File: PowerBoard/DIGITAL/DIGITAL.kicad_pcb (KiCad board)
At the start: 2 copper layers, 50 x 75 mm, 55 parts, among them J1 AuxConn, J2 Conn_02x02_Counter_Clockwise, Q2 BSS126, Q3 IRFR13N20DTRPBF, Q4 IRFR13N20DTRPBF, U3 MT2492, U4 TL431DBZ, U5 STM32G030F6Px, U6 IR2181, U7 INA180A2

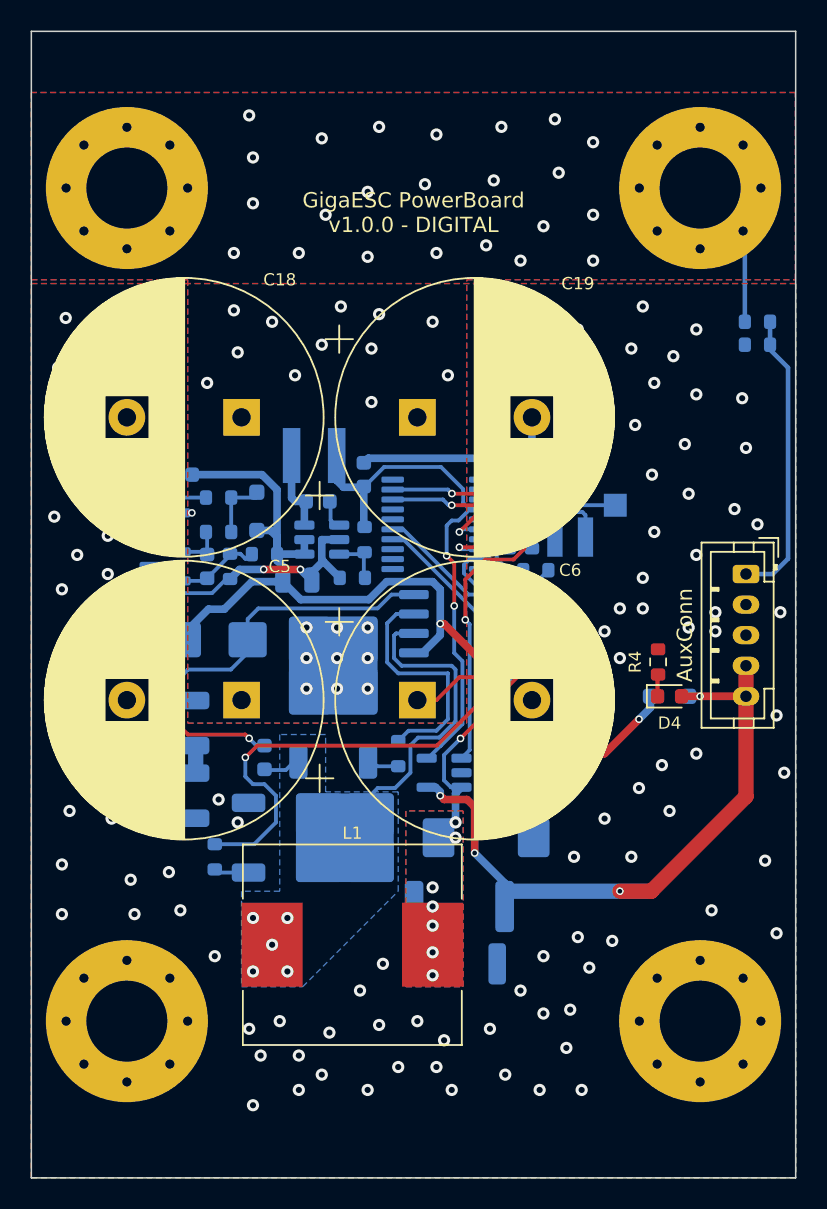
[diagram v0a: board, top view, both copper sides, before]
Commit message: v3.0.3 - Cosmetic Changes
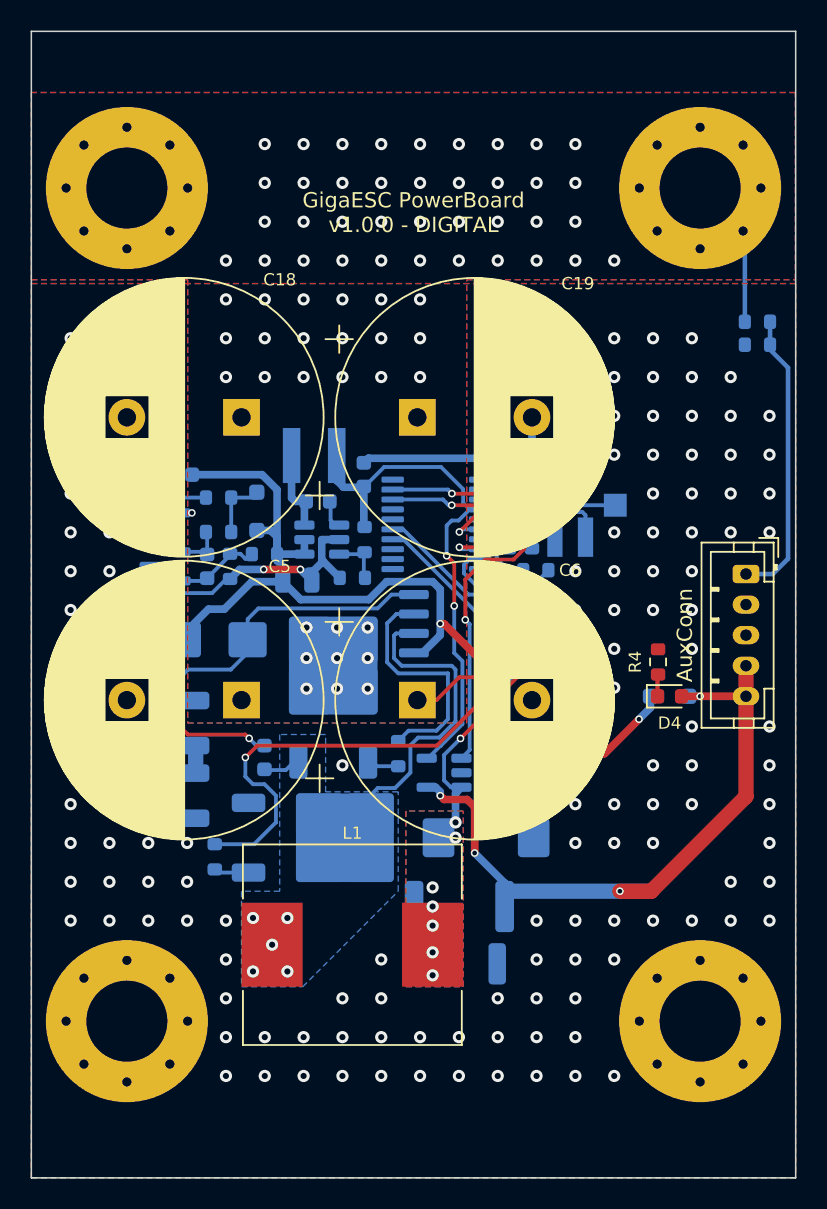
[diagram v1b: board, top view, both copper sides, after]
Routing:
- net -BATT: vias 115 -> 155
- net +BATT: vias 46 -> 67
